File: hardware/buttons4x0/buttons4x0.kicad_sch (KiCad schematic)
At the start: 11 parts, among them J1 Conn_01x05_Pin, SW1 Capacitive_Button, SW2 Capacitive_Button, SW3 Capacitive_Button, SW4 Capacitive_Button

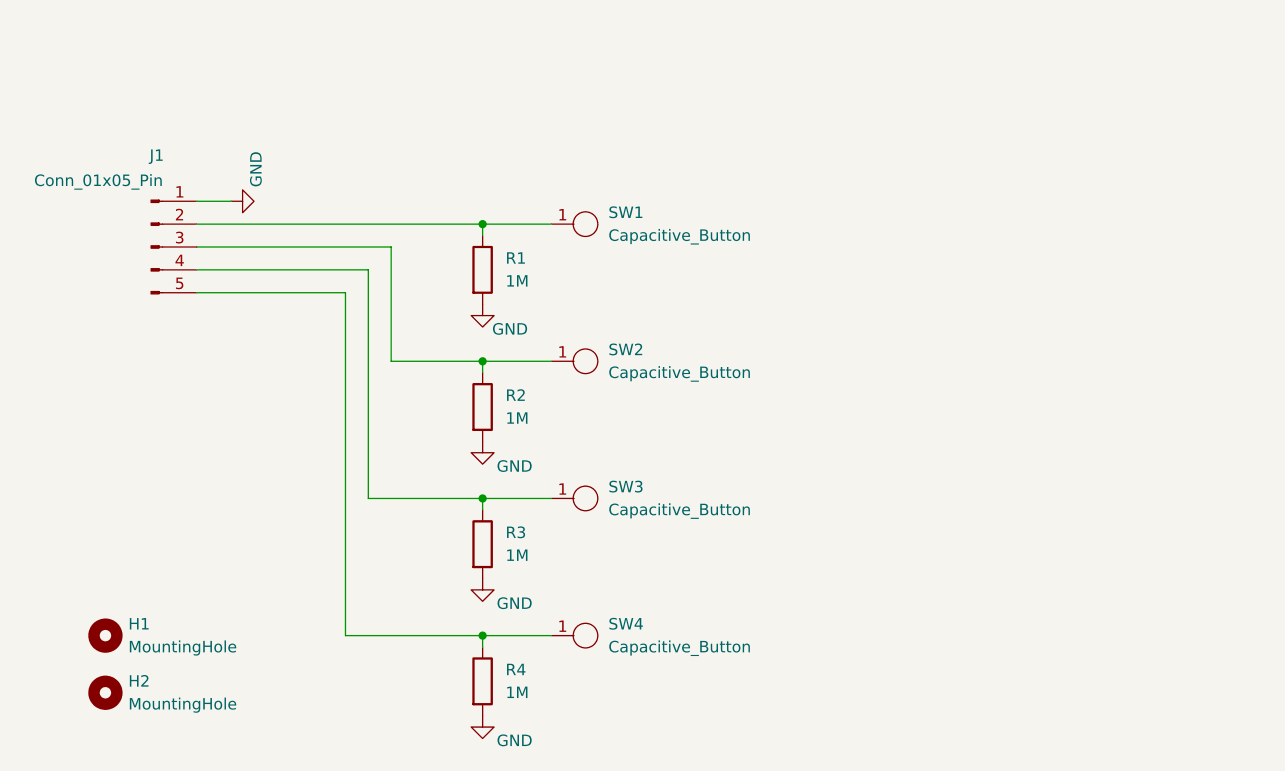
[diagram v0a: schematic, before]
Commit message: fix spacing to allow tiling a bit better
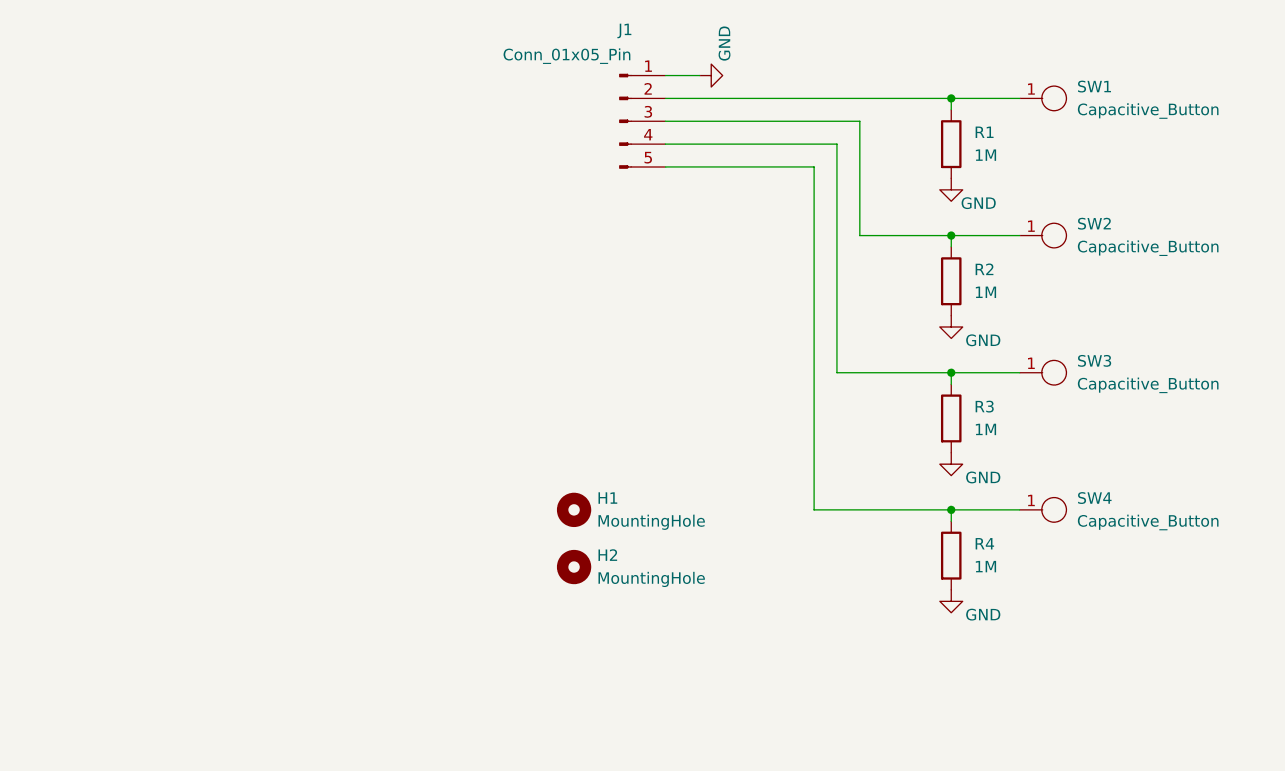
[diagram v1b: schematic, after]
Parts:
- SW1, SW2, SW3, SW4: footprint todbot_stuff:Pad-CapTouch-10mm-roundrect -> todbot_stuff:Pad-CapTouch-11_2mm-roundrect
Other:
- company: (none) -> todbot / Tod Kurt
- title: (none) -> buttons4x0
- moved on the sheet: H1, H2, J1, R1, R2, R3, R4, SW1, SW2, SW3, SW4
